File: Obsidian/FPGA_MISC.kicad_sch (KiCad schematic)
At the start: 21 parts, among them Q3 BSS138LT1G, SW1 SW_DIP_x01, U1 XC7A35T-CSG325, U27 S25FL128SAGMFI001, U9 REF3012

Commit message: Correct Schematic errors
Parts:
- C146, C150, C153, C154: footprint Capacitors SMD:CAPC0603X33N -> Footprint:CAPC0603X33N
- C151, C152: footprint Capacitors SMD:CAPC1005X70N -> Footprint:CAPC1005X70N
- L11: footprint Inductors SMD:INDC1608X95N -> Footprint:INDC1608X95N
- L15: footprint Inductors SMD:INDC2013X145N -> Footprint:INDC2013X145N
- LD5: footprint ICs And Semiconductors SMD:LED_KINGBRIGHT_KPH-1608CGCK -> Footprint:LED_KINGBRIGHT_KPH-1608CGCK
- Q3: footprint ICs And Semiconductors SMD:SOT95P240X110-3N -> Footprint:SOT95P240X110-3N
- R161, R85, R86, R87, R88, R89, R90: footprint Resistors SMD:RESC1005X40N -> Footprint:RESC1005X40N
- SW1: footprint Switches:SW_OMRON_A6SN-1101 -> Footprint:SW_OMRON_A6SN-1101
- U1: footprint Package_BGA:Xilinx_CSG325 -> Footprint:Xilinx_CSG325
- U27: footprint ICs And Semiconductors SMD:SOIC127P1030X265-16N -> Footprint:SOIC127P1030X265-16N
- U9: footprint Package_TO_SOT_SMD:SOT-23 -> Footprint:SOT-23
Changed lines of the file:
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@@
 			)
 		)
-		(property "Footprint" "Capacitors SMD:CAPC1005X70N"
+		(property "Footprint" "Footprint:CAPC1005X70N"
 			(at 168.148 138.43 0)
 			(effects
@@
 			)
 		)
-		(property "Footprint" "Package_TO_SOT_SMD:SOT-23"
+		(property "Footprint" "Footprint:SOT-23"
 			(at 189.23 149.86 0)
 			(effects
@@
 			)
 		)
-		(property "Footprint" "Capacitors SMD:CAPC0603X33N"
+		(property "Footprint" "Footprint:CAPC0603X33N"
 			(at 175.768 138.43 0)
 			(effects
@@
 			)
 		)
-		(property "Footprint" "Capacitors SMD:CAPC0603X33N"
+		(property "Footprint" "Footprint:CAPC0603X33N"
 			(at 102.108 46.99 0)
 			(effects
@@
 			)
 		)
-		(property "Footprint" "Package_BGA:Xilinx_CSG325"
+		(property "Footprint" "Footprint:Xilinx_CSG325"
 			(at 83.82 88.9 0)
 			(effects
@@
 			)
 		)
-		(property "Footprint" "Capacitors SMD:CAPC0603X33N"
+		(property "Footprint" "Footprint:CAPC0603X33N"
 			(at 133.35 146.558 0)
 			(effects
@@
 			)
 		)
-		(property "Footprint" "Capacitors SMD:CAPC1005X70N"
+		(property "Footprint" "Footprint:CAPC1005X70N"
 			(at 208.788 146.05 0)
 			(effects
@@
 			)
 		)
-		(property "Footprint" "Inductors SMD:INDC1608X95N"
+		(property "Footprint" "Footprint:INDC1608X95N"
 			(at 154.94 154.178 0)
 			(effects
@@
 			)
 		)
-		(property "Footprint" "Switches:SW_OMRON_A6SN-1101"
+		(property "Footprint" "Footprint:SW_OMRON_A6SN-1101"
 			(at 184.15 74.93 0)
 			(effects
@@
 			)
 		)
-		(property "Footprint" "Resistors SMD:RESC1005X40N"
+		(property "Footprint" "Footprint:RESC1005X40N"
 			(at 260.858 110.49 0)
 			(effects
@@
 			)
 		)
-		(property "Footprint" "Capacitors SMD:CAPC0603X33N"
+		(property "Footprint" "Footprint:CAPC0603X33N"
 			(at 110.998 46.99 0)
 			(effects
@@
 			)
 		)
-		(property "Footprint" "ICs And Semiconductors SMD:SOT95P240X110-3N"
+		(property "Footprint" "Footprint:SOT95P240X110-3N"
 			(at 247.65 133.858 0)
 			(effects
@@
 			)
 		)
-		(property "Footprint" "Resistors SMD:RESC1005X40N"
+		(property "Footprint" "Footprint:RESC1005X40N"
 			(at 166.878 83.82 0)
 			(effects
@@
 			)
 		)
-		(property "Footprint" "ICs And Semiconductors SMD:SOIC127P1030X265-16N"
+		(property "Footprint" "Footprint:SOIC127P1030X265-16N"
 			(at 220.98 93.98 0)
 			(effects
@@
 			)
 		)
-		(property "Footprint" "Resistors SMD:RESC1005X40N"
+		(property "Footprint" "Footprint:RESC1005X40N"
 			(at 157.48 82.042 0)
 			(effects
@@
 			)
 		)
-		(property "Footprint" "Resistors SMD:RESC1005X40N"
+		(property "Footprint" "Footprint:RESC1005X40N"
 			(at 157.48 79.502 0)
 			(effects
@@
 			)
 		)
-		(property "Footprint" "Resistors SMD:RESC1005X40N"
+		(property "Footprint" "Footprint:RESC1005X40N"
 			(at 188.468 91.44 0)
 			(effects
@@
 			)
 		)
-		(property "Footprint" "Resistors SMD:RESC1005X40N"
+		(property "Footprint" "Footprint:RESC1005X40N"
 			(at 175.768 91.44 0)
 			(effects
@@
 			)
 		)
-		(property "Footprint" "Resistors SMD:RESC1005X40N"
+		(property "Footprint" "Footprint:RESC1005X40N"
 			(at 182.118 91.44 0)
 			(effects
@@
 			)
 		)
-		(property "Footprint" "ICs And Semiconductors SMD:LED_KINGBRIGHT_KPH-1608CGCK"
+		(property "Footprint" "Footprint:LED_KINGBRIGHT_KPH-1608CGCK"
 			(at 246.634 114.3 0)
 			(effects
@@
 			)
 		)
-		(property "Footprint" "Inductors SMD:INDC2013X145N"
+		(property "Footprint" "Footprint:INDC2013X145N"
 			(at 149.86 137.16 0)
 			(effects

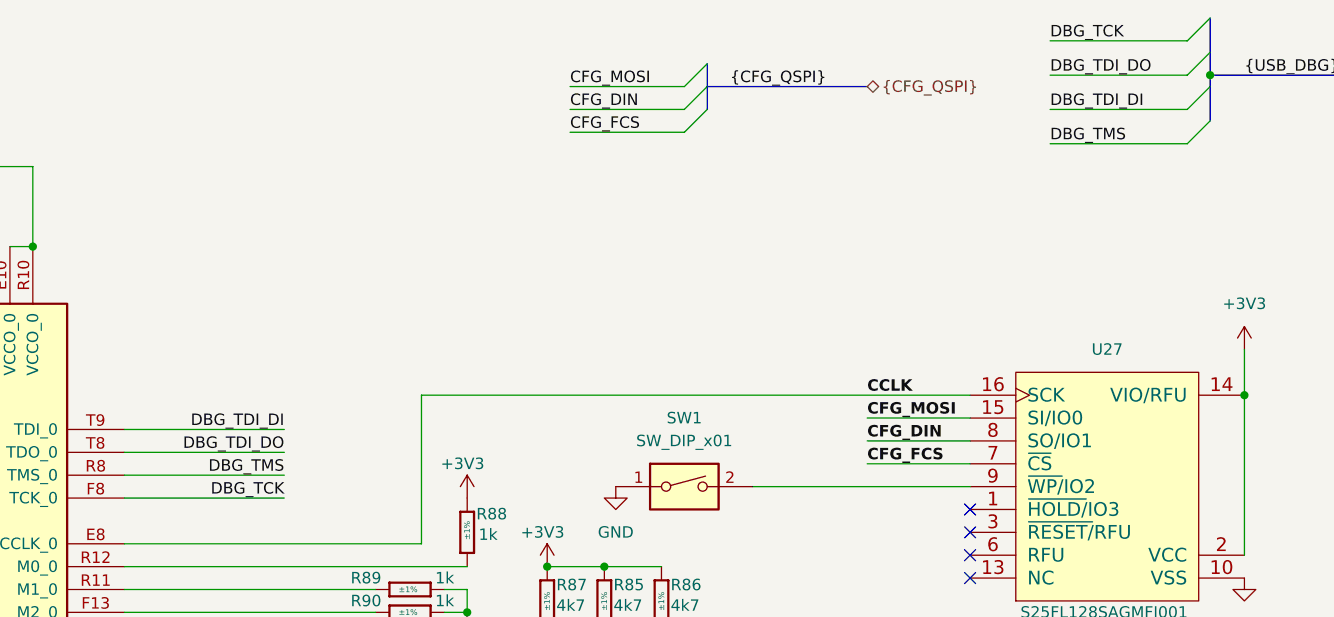
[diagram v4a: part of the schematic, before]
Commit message: correcting mismatch in TX/RX of UART
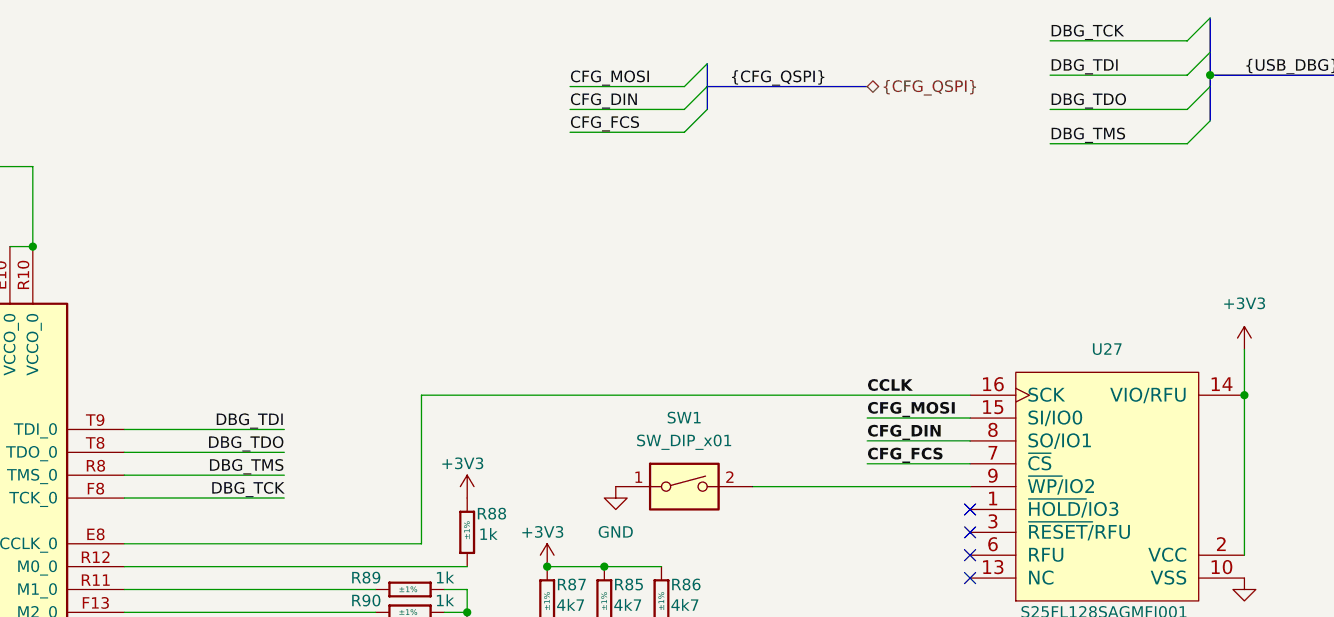
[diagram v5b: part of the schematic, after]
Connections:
- net DBG_TDI_DI renamed DBG_TDI
- net DBG_TDI_DO renamed DBG_TDO
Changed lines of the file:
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@@
 		)
 	)
-	(label "DBG_TDI_DI"
+	(label "DBG_TDI"
 		(at 139.7 68.58 180)
 		(effects
@@
 		)
 	)
-	(label "DBG_TDI_DO"
+	(label "DBG_TDI"
 		(at 224.79 29.21 0)
 		(effects
@@
 		)
 	)
-	(label "DBG_TDI_DO"
+	(label "DBG_TDO"
 		(at 139.7 71.12 180)
 		(effects
@@
 		)
 	)
-	(label "DBG_TDI_DI"
+	(label "DBG_TDO"
 		(at 224.79 33.02 0)
 		(effects

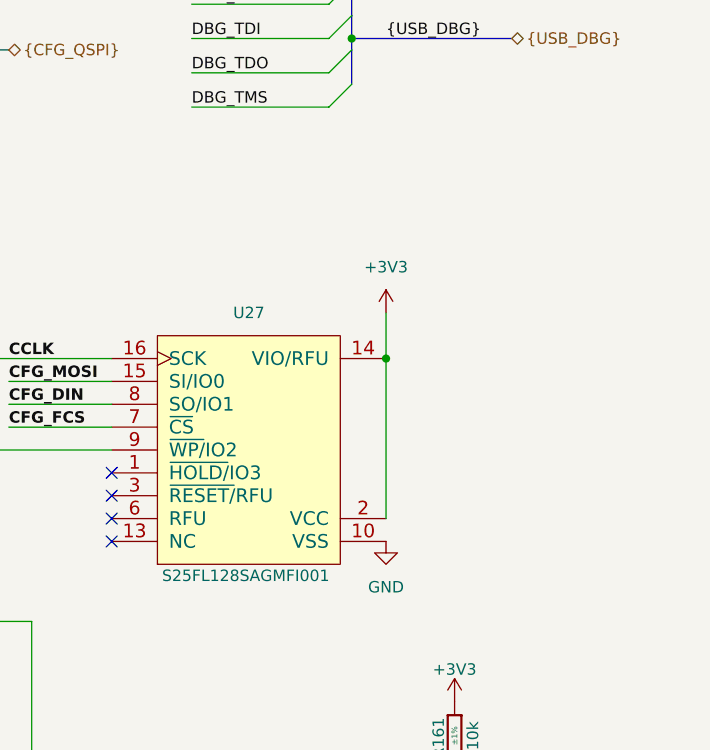
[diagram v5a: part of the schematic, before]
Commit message: adding 3D files, 3D model of twist, and correct DRC
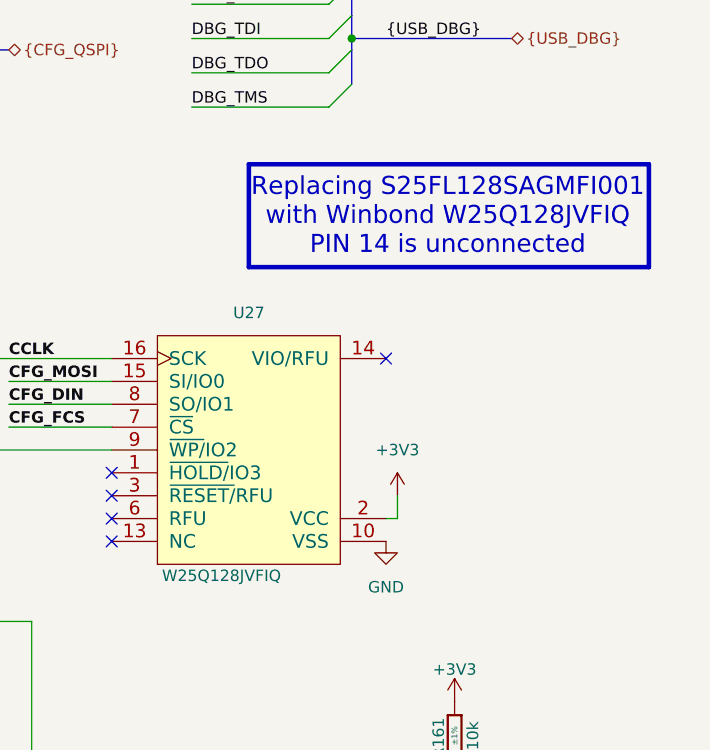
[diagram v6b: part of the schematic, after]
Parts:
- U27: value S25FL128SAGMFI001 -> W25Q128JVFIQ; Library Ref S25FL128SAGMFI001 -> W25Q128JVFIQ; Part Number S25FL128SAGMFI001 -> W25Q128JVFIQ
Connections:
- net +3V3: no longer U27.14 (VIO/RFU)
- no-connect marks 4 -> 5
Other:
- note added: "Replacing S25FL128SAGMFI001 with Winbond W25Q128JVFIQ PIN 14 is unconnected"
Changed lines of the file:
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@@
 		(members "CFG_MOSI" "CFG_DIN" "CFG_FCS")
 	)
+	(rectangle
+		(start 231.14 43.18)
+		(end 275.59 54.61)
+		(stroke
+			(width 0.5)
+			(type solid)
+			(color 255 0 0 1)
+		)
+		(fill
+			(type none)
+		)
+	)
 	(text "FPGA DONE"
 		(exclude_from_sim no)
@@
 		)
 	)
+	(text "Replacing S25FL128SAGMFI001 \nwith Winbond W25Q128JVFIQ\nPIN 14 is unconnected"
+		(exclude_from_sim no)
+		(at 253.238 49.022 0)
+		(effects
+			(font
+				(size 2 2)
+			)
+		)
+	)
 	(junction
 		(at 129.54 119.38)
@@
 	)
 	(junction
-		(at 246.38 64.77)
-		(diameter 0)
-		(color 0 0 0 0)
-	)
-	(junction
 		(at 175.26 83.82)
 		(diameter 0)
@@
 	)
 	(no_connect
+		(at 246.38 64.77)
+	)
+	(no_connect
 		(at 215.9 82.55)
 	)
@@
 	(wire
 		(pts
+			(xy 247.65 82.55) (xy 246.38 82.55)
+		)
+		(stroke
+			(width 0)
+			(type default)
+		)
+	)
+	(wire
+		(pts
 			(xy 160.02 138.43) (xy 167.64 138.43)
 		)
@@
 	(wire
 		(pts
-			(xy 246.38 64.77) (xy 246.38 82.55)
-		)
-		(stroke
-			(width 0)
-			(type default)
-		)
-	)
-	(wire
-		(pts
 			(xy 167.64 130.81) (xy 186.69 130.81)
 		)
@@
 	(wire
 		(pts
-			(xy 246.38 59.69) (xy 246.38 64.77)
-		)
-		(stroke
-			(width 0)
-			(type default)
-		)
-	)
-	(wire
-		(pts
 			(xy 168.91 96.52) (xy 168.91 91.44)
 		)
@@
 	(wire
 		(pts
+			(xy 247.65 80.01) (xy 247.65 82.55)
+		)
+		(stroke
+			(width 0)
+			(type default)
+		)
+	)
+	(wire
+		(pts
 			(xy 204.47 69.85) (xy 215.9 69.85)
 		)
@@
 			)
 		)
-		(property "Value" "S25FL128SAGMFI001"
+		(property "Value" "W25Q128JVFIQ"
 			(at 221.488 88.9 0)
 			(effects
@@
 			)
 		)
-		(property "Datasheet" "\\\\cern.ch\\dfs\\Applications\\Altium\\Datasheets\\S25FL128SAGMFI001.pdf"
+		(property "Datasheet" "https://www.lcsc.com/datasheet/C111478.pdf"
 			(at 220.98 95.885 0)
 			(effects
@@
 			)
 		)
-		(property "Part Number" "S25FL128SAGMFI001"
+		(property "Part Number" "W25Q128JVFIQ "
 			(at 220.98 97.79 0)
 			(effects
@@
 			)
 		)
-		(property "Library Ref" "S25FL128SAGMFI001"
+		(property "Library Ref" "W25Q128JVFIQ "
 			(at 220.98 99.695 0)
 			(effects
@@
 	(symbol
 		(lib_id "Library_Symbol:+1V0")
-		(at 246.38 59.69 0)
+		(at 247.65 80.01 0)
 		(unit 1)
 		(exclude_from_sim no)
@@
 		(fields_autoplaced yes)
 		(property "Reference" "#PWR0130"
-			(at 246.38 63.5 0)
+			(at 247.65 83.82 0)
 			(effects
 				(font
@@
 		)
 		(property "Value" "+3V3"
-			(at 246.38 54.61 0)
+			(at 247.65 74.93 0)
 			(effects
 				(font
@@
 		)
 		(property "Footprint" ""
-			(at 246.38 59.69 0)
+			(at 247.65 80.01 0)
 			(effects
 				(font
@@
 		)
 		(property "Datasheet" ""
-			(at 246.38 59.69 0)
+			(at 247.65 80.01 0)
 			(effects
 				(font
@@
 		)
 		(property "Description" "Power symbol creates a global label with name \"+1V0\""
-			(at 246.38 59.69 0)
+			(at 247.65 80.01 0)
 			(effects
 				(font
